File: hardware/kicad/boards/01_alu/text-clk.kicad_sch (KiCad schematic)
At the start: 8 parts, among them U287 ICM7555xB, U288 74HCT541

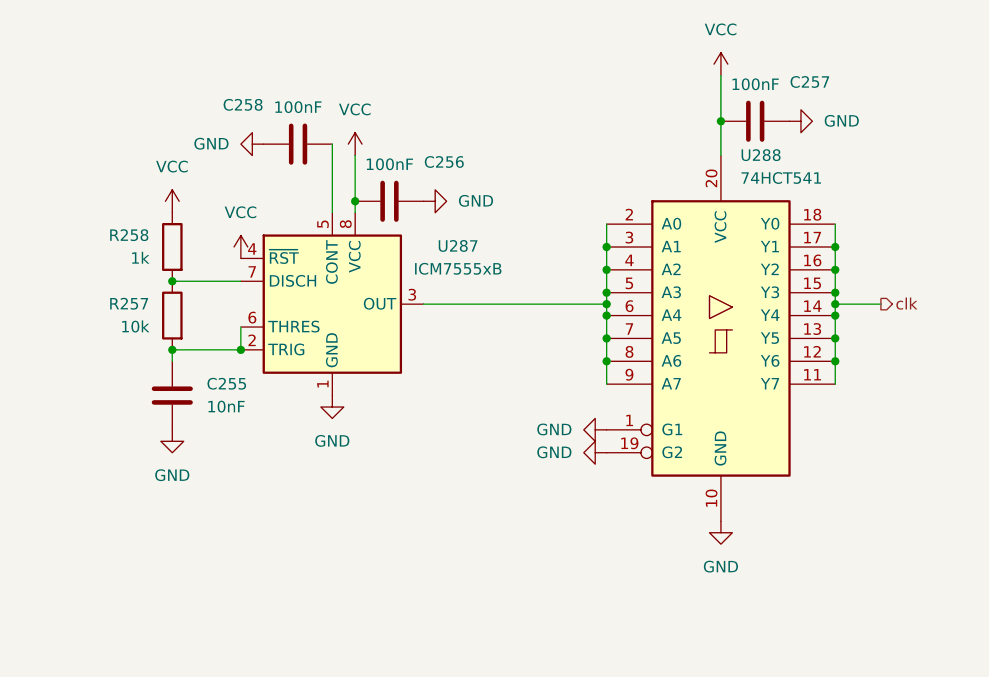
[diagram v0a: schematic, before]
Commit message: kicad: checkpoint; designed the alu display logic; clock circuit
Added registers for each display to ensure robustness and less worry about debugging screen, keeping focus on the alu board and other components
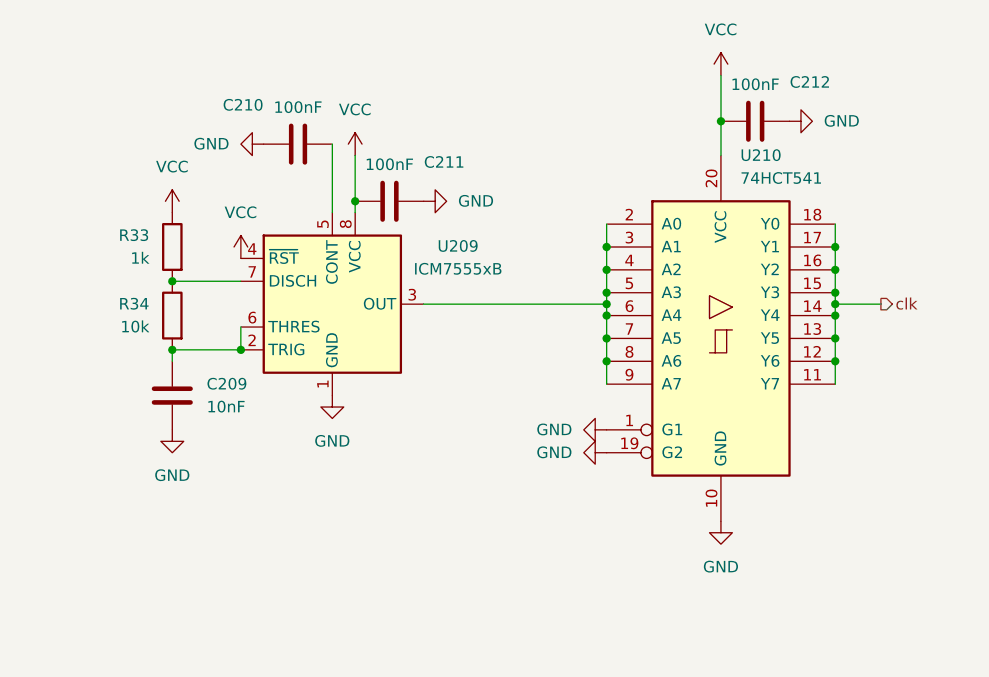
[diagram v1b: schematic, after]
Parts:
- renumbered C255 to C209, C258 to C210, C256 to C211, C257 to C212, R258 to R33, R257 to R34, U287 to U209, U288 to U210
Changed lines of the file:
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@@
 		(instances
 			(project "alu-32b"
-				(path "/ddad1417-0afc-402d-a021-92fc87ddd78a/6de98612-1f6c-44a2-b1a6-09346f0d4282/54a30aeb-1148-4a28-8e36-f59c82c9762f"
+				(path "/ddad1417-0afc-402d-a021-92fc87ddd78a/70179ff6-7c16-4036-adf3-4ea9b5e0a238/54a30aeb-1148-4a28-8e36-f59c82c9762f"
 					(reference "#PWR01036")
 					(unit 1)
@@
 		(dnp no)
 		(fields_autoplaced yes)
-		(property "Reference" "U288"
+		(property "Reference" "U210"
 			(at 173.5933 43.18 0)
 			(show_name no)
@@
 		(instances
 			(project "alu-32b"
-				(path "/ddad1417-0afc-402d-a021-92fc87ddd78a/6de98612-1f6c-44a2-b1a6-09346f0d4282/54a30aeb-1148-4a28-8e36-f59c82c9762f"
-					(reference "U288")
+				(path "/ddad1417-0afc-402d-a021-92fc87ddd78a/70179ff6-7c16-4036-adf3-4ea9b5e0a238/54a30aeb-1148-4a28-8e36-f59c82c9762f"
+					(reference "U210")
 					(unit 1)
 				)
@@
 		(instances
 			(project "alu-32b"
-				(path "/ddad1417-0afc-402d-a021-92fc87ddd78a/6de98612-1f6c-44a2-b1a6-09346f0d4282/54a30aeb-1148-4a28-8e36-f59c82c9762f"
+				(path "/ddad1417-0afc-402d-a021-92fc87ddd78a/70179ff6-7c16-4036-adf3-4ea9b5e0a238/54a30aeb-1148-4a28-8e36-f59c82c9762f"
 					(reference "#PWR01042")
 					(unit 1)
@@
 		(in_pos_files yes)
 		(dnp no)
-		(property "Reference" "C258"
+		(property "Reference" "C210"
 			(at 118.364 37.592 90)
 			(show_name no)
@@
 		(instances
 			(project "alu-32b"
-				(path "/ddad1417-0afc-402d-a021-92fc87ddd78a/6de98612-1f6c-44a2-b1a6-09346f0d4282/54a30aeb-1148-4a28-8e36-f59c82c9762f"
-					(reference "C258")
+				(path "/ddad1417-0afc-402d-a021-92fc87ddd78a/70179ff6-7c16-4036-adf3-4ea9b5e0a238/54a30aeb-1148-4a28-8e36-f59c82c9762f"
+					(reference "C210")
 					(unit 1)
 				)
@@
 		(in_pos_files yes)
 		(dnp no)
-		(property "Reference" "R258"
+		(property "Reference" "R33"
 			(at 107.95 52.0699 0)
 			(show_name no)
@@
 		(instances
 			(project "alu-32b"
-				(path "/ddad1417-0afc-402d-a021-92fc87ddd78a/6de98612-1f6c-44a2-b1a6-09346f0d4282/54a30aeb-1148-4a28-8e36-f59c82c9762f"
-					(reference "R258")
+				(path "/ddad1417-0afc-402d-a021-92fc87ddd78a/70179ff6-7c16-4036-adf3-4ea9b5e0a238/54a30aeb-1148-4a28-8e36-f59c82c9762f"
+					(reference "R33")
 					(unit 1)
 				)
@@
 		(dnp no)
 		(fields_autoplaced yes)
-		(property "Reference" "U287"
+		(property "Reference" "U209"
 			(at 142.24 53.2698 0)
 			(show_name no)
@@
 		(instances
 			(project "alu-32b"
-				(path "/ddad1417-0afc-402d-a021-92fc87ddd78a/6de98612-1f6c-44a2-b1a6-09346f0d4282/54a30aeb-1148-4a28-8e36-f59c82c9762f"
-					(reference "U287")
+				(path "/ddad1417-0afc-402d-a021-92fc87ddd78a/70179ff6-7c16-4036-adf3-4ea9b5e0a238/54a30aeb-1148-4a28-8e36-f59c82c9762f"
+					(reference "U209")
 					(unit 1)
 				)
@@
 		(instances
 			(project "alu-32b"
-				(path "/ddad1417-0afc-402d-a021-92fc87ddd78a/6de98612-1f6c-44a2-b1a6-09346f0d4282/54a30aeb-1148-4a28-8e36-f59c82c9762f"
+				(path "/ddad1417-0afc-402d-a021-92fc87ddd78a/70179ff6-7c16-4036-adf3-4ea9b5e0a238/54a30aeb-1148-4a28-8e36-f59c82c9762f"
 					(reference "#PWR01031")
 					(unit 1)
@@
 		(in_pos_files yes)
 		(dnp no)
-		(property "Reference" "C257"
+		(property "Reference" "C212"
 			(at 181.356 35.052 90)
 			(show_name no)
@@
 		(instances
 			(project "alu-32b"
-				(path "/ddad1417-0afc-402d-a021-92fc87ddd78a/6de98612-1f6c-44a2-b1a6-09346f0d4282/54a30aeb-1148-4a28-8e36-f59c82c9762f"
-					(reference "C257")
+				(path "/ddad1417-0afc-402d-a021-92fc87ddd78a/70179ff6-7c16-4036-adf3-4ea9b5e0a238/54a30aeb-1148-4a28-8e36-f59c82c9762f"
+					(reference "C212")
 					(unit 1)
 				)
@@
 		(in_pos_files yes)
 		(dnp no)
-		(property "Reference" "R257"
+		(property "Reference" "R34"
 			(at 107.95 59.6899 0)
 			(show_name no)
@@
 		(instances
 			(project "alu-32b"
-				(path "/ddad1417-0afc-402d-a021-92fc87ddd78a/6de98612-1f6c-44a2-b1a6-09346f0d4282/54a30aeb-1148-4a28-8e36-f59c82c9762f"
-					(reference "R257")
+				(path "/ddad1417-0afc-402d-a021-92fc87ddd78a/70179ff6-7c16-4036-adf3-4ea9b5e0a238/54a30aeb-1148-4a28-8e36-f59c82c9762f"
+					(reference "R34")
 					(unit 1)
 				)
@@
 		(instances
 			(project "alu-32b"
-				(path "/ddad1417-0afc-402d-a021-92fc87ddd78a/6de98612-1f6c-44a2-b1a6-09346f0d4282/54a30aeb-1148-4a28-8e36-f59c82c9762f"
+				(path "/ddad1417-0afc-402d-a021-92fc87ddd78a/70179ff6-7c16-4036-adf3-4ea9b5e0a238/54a30aeb-1148-4a28-8e36-f59c82c9762f"
 					(reference "#PWR01032")
 					(unit 1)
@@
 		(instances
 			(project "alu-32b"
-				(path "/ddad1417-0afc-402d-a021-92fc87ddd78a/6de98612-1f6c-44a2-b1a6-09346f0d4282/54a30aeb-1148-4a28-8e36-f59c82c9762f"
+				(path "/ddad1417-0afc-402d-a021-92fc87ddd78a/70179ff6-7c16-4036-adf3-4ea9b5e0a238/54a30aeb-1148-4a28-8e36-f59c82c9762f"
 					(reference "#PWR01037")
 					(unit 1)
@@
 		(instances
 			(project "alu-32b"
-				(path "/ddad1417-0afc-402d-a021-92fc87ddd78a/6de98612-1f6c-44a2-b1a6-09346f0d4282/54a30aeb-1148-4a28-8e36-f59c82c9762f"
+				(path "/ddad1417-0afc-402d-a021-92fc87ddd78a/70179ff6-7c16-4036-adf3-4ea9b5e0a238/54a30aeb-1148-4a28-8e36-f59c82c9762f"
 					(reference "#PWR01039")
 					(unit 1)
@@
 		(instances
 			(project "alu-32b"
-				(path "/ddad1417-0afc-402d-a021-92fc87ddd78a/6de98612-1f6c-44a2-b1a6-09346f0d4282/54a30aeb-1148-4a28-8e36-f59c82c9762f"
+				(path "/ddad1417-0afc-402d-a021-92fc87ddd78a/70179ff6-7c16-4036-adf3-4ea9b5e0a238/54a30aeb-1148-4a28-8e36-f59c82c9762f"
 					(reference "#PWR01040")
 					(unit 1)
@@
 		(instances
 			(project "alu-32b"
-				(path "/ddad1417-0afc-402d-a021-92fc87ddd78a/6de98612-1f6c-44a2-b1a6-09346f0d4282/54a30aeb-1148-4a28-8e36-f59c82c9762f"
+				(path "/ddad1417-0afc-402d-a021-92fc87ddd78a/70179ff6-7c16-4036-adf3-4ea9b5e0a238/54a30aeb-1148-4a28-8e36-f59c82c9762f"
 					(reference "#PWR01034")
 					(unit 1)
@@
 		(instances
 			(project "alu-32b"
-				(path "/ddad1417-0afc-402d-a021-92fc87ddd78a/6de98612-1f6c-44a2-b1a6-09346f0d4282/54a30aeb-1148-4a28-8e36-f59c82c9762f"
+				(path "/ddad1417-0afc-402d-a021-92fc87ddd78a/70179ff6-7c16-4036-adf3-4ea9b5e0a238/54a30aeb-1148-4a28-8e36-f59c82c9762f"
 					(reference "#PWR01033")
 					(unit 1)
@@
 		(instances
 			(project "alu-32b"
-				(path "/ddad1417-0afc-402d-a021-92fc87ddd78a/6de98612-1f6c-44a2-b1a6-09346f0d4282/54a30aeb-1148-4a28-8e36-f59c82c9762f"
+				(path "/ddad1417-0afc-402d-a021-92fc87ddd78a/70179ff6-7c16-4036-adf3-4ea9b5e0a238/54a30aeb-1148-4a28-8e36-f59c82c9762f"
 					(reference "#PWR01038")
 					(unit 1)
@@
 		(instances
 			(project "alu-32b"
-				(path "/ddad1417-0afc-402d-a021-92fc87ddd78a/6de98612-1f6c-44a2-b1a6-09346f0d4282/54a30aeb-1148-4a28-8e36-f59c82c9762f"
+				(path "/ddad1417-0afc-402d-a021-92fc87ddd78a/70179ff6-7c16-4036-adf3-4ea9b5e0a238/54a30aeb-1148-4a28-8e36-f59c82c9762f"
 					(reference "#PWR01041")
 					(unit 1)
@@
 		(dnp no)
 		(fields_autoplaced yes)
-		(property "Reference" "C255"
+		(property "Reference" "C209"
 			(at 114.3 68.5799 0)
 			(show_name no)
@@
 		(instances
 			(project "alu-32b"
-				(path "/ddad1417-0afc-402d-a021-92fc87ddd78a/6de98612-1f6c-44a2-b1a6-09346f0d4282/54a30aeb-1148-4a28-8e36-f59c82c9762f"
-					(reference "C255")
+				(path "/ddad1417-0afc-402d-a021-92fc87ddd78a/70179ff6-7c16-4036-adf3-4ea9b5e0a238/54a30aeb-1148-4a28-8e36-f59c82c9762f"
+					(reference "C209")
 					(unit 1)
 				)
@@
 		(in_pos_files yes)
 		(dnp no)
-		(property "Reference" "C256"
+		(property "Reference" "C211"
 			(at 140.716 43.942 90)
 			(show_name no)
@@
 		(instances
 			(project "alu-32b"
-				(path "/ddad1417-0afc-402d-a021-92fc87ddd78a/6de98612-1f6c-44a2-b1a6-09346f0d4282/54a30aeb-1148-4a28-8e36-f59c82c9762f"
-					(reference "C256")
+				(path "/ddad1417-0afc-402d-a021-92fc87ddd78a/70179ff6-7c16-4036-adf3-4ea9b5e0a238/54a30aeb-1148-4a28-8e36-f59c82c9762f"
+					(reference "C211")
 					(unit 1)
 				)
@@
 		(instances
 			(project "alu-32b"
-				(path "/ddad1417-0afc-402d-a021-92fc87ddd78a/6de98612-1f6c-44a2-b1a6-09346f0d4282/54a30aeb-1148-4a28-8e36-f59c82c9762f"
+				(path "/ddad1417-0afc-402d-a021-92fc87ddd78a/70179ff6-7c16-4036-adf3-4ea9b5e0a238/54a30aeb-1148-4a28-8e36-f59c82c9762f"
 					(reference "#PWR01035")
 					(unit 1)

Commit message: alu: completed all core schematics; DRC and ERC pending 🎉
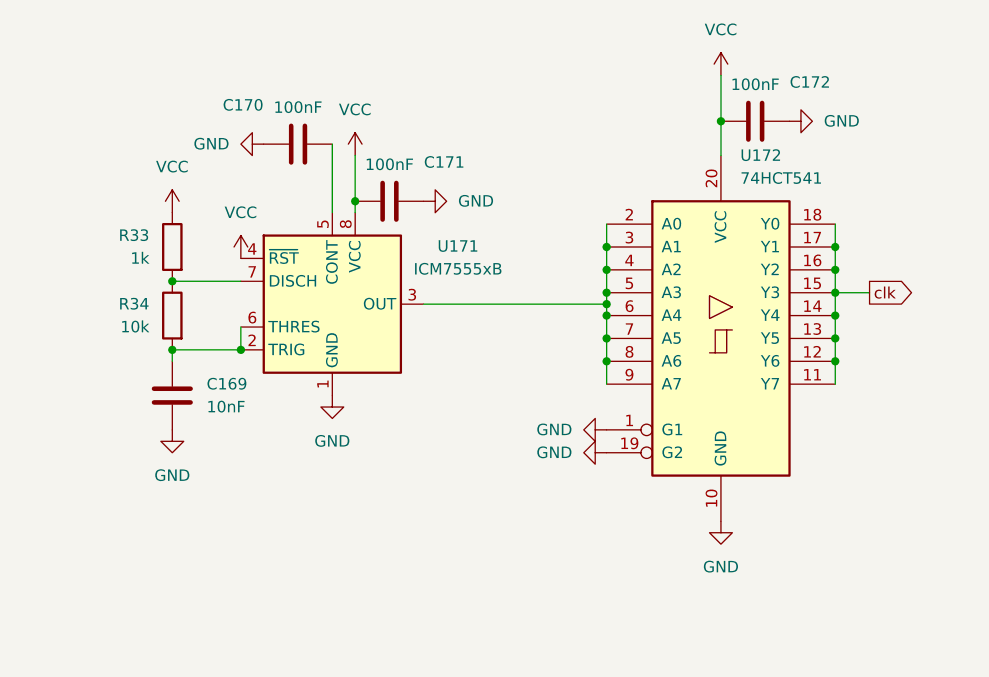
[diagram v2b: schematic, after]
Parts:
- U172: renamed from U210; footprint (none) -> Package_SO:SOIC-20W_7.5x12.8mm_P1.27mm
- renumbered C209 to C169, C210 to C170, C211 to C171, C212 to C172, U209 to U171
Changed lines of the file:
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@@
-	)
-	(junction
-		(at 184.15 59.69)
-		(diameter 0)
-		(color 0 0 0 0)
 	)
 	(junction
@@
 	(wire
 		(pts
-			(xy 184.15 59.69) (xy 184.15 60.96)
+			(xy 184.15 58.42) (xy 184.15 60.96)
 		)
 		(stroke
@@
 	(wire
 		(pts
+			(xy 184.15 58.42) (xy 187.96 58.42)
+		)
+		(stroke
+			(width 0)
+			(type default)
+		)
+	)
+	(wire
+		(pts
 			(xy 184.15 60.96) (xy 184.15 63.5)
 		)
@@
 	(wire
 		(pts
-			(xy 184.15 59.69) (xy 189.23 59.69)
-		)
-		(stroke
-			(width 0)
-			(type default)
-		)
-	)
-	(wire
-		(pts
 			(xy 158.75 59.69) (xy 158.75 60.96)
 		)
@@
 	(wire
 		(pts
-			(xy 184.15 58.42) (xy 184.15 59.69)
-		)
-		(stroke
-			(width 0)
-			(type default)
-		)
-	)
-	(wire
-		(pts
 			(xy 110.49 66.04) (xy 110.49 64.77)
 		)
@@
 		)
 	)
-	(hierarchical_label "clk"
+	(global_label "clk"
 		(shape output)
-		(at 189.23 59.69 0)
+		(at 187.96 58.42 0)
+		(fields_autoplaced yes)
 		(effects
 			(font
@@
 			(justify left)
 		)
+		(property "Intersheetrefs" "${INTERSHEET_REFS}"
+			(at 193.7271 58.42 0)
+			(hide yes)
+			(show_name no)
+			(do_not_autoplace no)
+			(effects
+				(font
+					(size 1.27 1.27)
+				)
+				(justify left)
+			)
+		)
 	)
 	(symbol
@@
 		(dnp no)
 		(fields_autoplaced yes)
-		(property "Reference" "#PWR01036"
+		(property "Reference" "#PWR0667"
 			(at 110.49 53.34 0)
 			(hide yes)
@@
 			(project "alu-32b"
 				(path "/ddad1417-0afc-402d-a021-92fc87ddd78a/70179ff6-7c16-4036-adf3-4ea9b5e0a238/54a30aeb-1148-4a28-8e36-f59c82c9762f"
-					(reference "#PWR01036")
+					(reference "#PWR0667")
 					(unit 1)
 				)
@@
 		(dnp no)
 		(fields_autoplaced yes)
-		(property "Reference" "U210"
+		(property "Reference" "U172"
 			(at 173.5933 43.18 0)
 			(show_name no)
@@
 			)
 		)
-		(property "Footprint" ""
+		(property "Footprint" "Package_SO:SOIC-20W_7.5x12.8mm_P1.27mm"
 			(at 171.45 63.5 0)
 			(hide yes)
@@
 			(project "alu-32b"
 				(path "/ddad1417-0afc-402d-a021-92fc87ddd78a/70179ff6-7c16-4036-adf3-4ea9b5e0a238/54a30aeb-1148-4a28-8e36-f59c82c9762f"
-					(reference "U210")
+					(reference "U172")
 					(unit 1)
 				)
@@
 		(dnp no)
 		(fields_autoplaced yes)
-		(property "Reference" "#PWR01042"
+		(property "Reference" "#PWR0670"
 			(at 114.3 41.91 0)
 			(hide yes)
@@
 			(project "alu-32b"
 				(path "/ddad1417-0afc-402d-a021-92fc87ddd78a/70179ff6-7c16-4036-adf3-4ea9b5e0a238/54a30aeb-1148-4a28-8e36-f59c82c9762f"
-					(reference "#PWR01042")
+					(reference "#PWR0670")
 					(unit 1)
 				)
@@
 		(in_pos_files yes)
 		(dnp no)
-		(property "Reference" "C210"
+		(property "Reference" "C170"
 			(at 118.364 37.592 90)
 			(show_name no)
@@
 			(project "alu-32b"
 				(path "/ddad1417-0afc-402d-a021-92fc87ddd78a/70179ff6-7c16-4036-adf3-4ea9b5e0a238/54a30aeb-1148-4a28-8e36-f59c82c9762f"
-					(reference "C210")
+					(reference "C170")
 					(unit 1)
 				)
@@
 		(dnp no)
 		(fields_autoplaced yes)
-		(property "Reference" "U209"
+		(property "Reference" "U171"
 			(at 142.24 53.2698 0)
 			(show_name no)
@@
 			(project "alu-32b"
 				(path "/ddad1417-0afc-402d-a021-92fc87ddd78a/70179ff6-7c16-4036-adf3-4ea9b5e0a238/54a30aeb-1148-4a28-8e36-f59c82c9762f"
-					(reference "U209")
+					(reference "U171")
 					(unit 1)
 				)
@@
 		(dnp no)
 		(fields_autoplaced yes)
-		(property "Reference" "#PWR01031"
+		(property "Reference" "#PWR0671"
 			(at 128.27 76.2 0)
 			(hide yes)
@@
 			(project "alu-32b"
 				(path "/ddad1417-0afc-402d-a021-92fc87ddd78a/70179ff6-7c16-4036-adf3-4ea9b5e0a238/54a30aeb-1148-4a28-8e36-f59c82c9762f"
-					(reference "#PWR01031")
+					(reference "#PWR0671")
 					(unit 1)
 				)
@@
 		(in_pos_files yes)
 		(dnp no)
-		(property "Reference" "C212"
+		(property "Reference" "C172"
 			(at 181.356 35.052 90)
 			(show_name no)
@@
 			(project "alu-32b"
 				(path "/ddad1417-0afc-402d-a021-92fc87ddd78a/70179ff6-7c16-4036-adf3-4ea9b5e0a238/54a30aeb-1148-4a28-8e36-f59c82c9762f"
-					(reference "C212")
+					(reference "C172")
 					(unit 1)
 				)
@@
 		(dnp no)
 		(fields_autoplaced yes)
-		(property "Reference" "#PWR01032"
+		(property "Reference" "#PWR0669"
 			(at 118.11 58.42 0)
 			(hide yes)
@@
 			(project "alu-32b"
 				(path "/ddad1417-0afc-402d-a021-92fc87ddd78a/70179ff6-7c16-4036-adf3-4ea9b5e0a238/54a30aeb-1148-4a28-8e36-f59c82c9762f"
-					(reference "#PWR01032")
+					(reference "#PWR0669")
 					(unit 1)
 				)
@@
 		(dnp no)
 		(fields_autoplaced yes)
-		(property "Reference" "#PWR01037"
+		(property "Reference" "#PWR0677"
 			(at 171.45 90.17 0)
 			(hide yes)
@@
 			(project "alu-32b"
 				(path "/ddad1417-0afc-402d-a021-92fc87ddd78a/70179ff6-7c16-4036-adf3-4ea9b5e0a238/54a30aeb-1148-4a28-8e36-f59c82c9762f"
-					(reference "#PWR01037")
+					(reference "#PWR0677")
 					(unit 1)
 				)
@@
 		(dnp no)
 		(fields_autoplaced yes)
-		(property "Reference" "#PWR01039"
+		(property "Reference" "#PWR0675"
 			(at 152.4 76.2 0)
 			(hide yes)
@@
 			(project "alu-32b"
 				(path "/ddad1417-0afc-402d-a021-92fc87ddd78a/70179ff6-7c16-4036-adf3-4ea9b5e0a238/54a30aeb-1148-4a28-8e36-f59c82c9762f"
-					(reference "#PWR01039")
+					(reference "#PWR0675")
 					(unit 1)
 				)
@@
 		(dnp no)
 		(fields_autoplaced yes)
-		(property "Reference" "#PWR01040"
+		(property "Reference" "#PWR0676"
 			(at 171.45 38.1 0)
 			(hide yes)
@@
 			(project "alu-32b"
 				(path "/ddad1417-0afc-402d-a021-92fc87ddd78a/70179ff6-7c16-4036-adf3-4ea9b5e0a238/54a30aeb-1148-4a28-8e36-f59c82c9762f"
-					(reference "#PWR01040")
+					(reference "#PWR0676")
 					(unit 1)
 				)
@@
 		(dnp no)
 		(fields_autoplaced yes)
-		(property "Reference" "#PWR01034"
+		(property "Reference" "#PWR0673"
 			(at 144.78 48.26 0)
 			(hide yes)
@@
 			(project "alu-32b"
 				(path "/ddad1417-0afc-402d-a021-92fc87ddd78a/70179ff6-7c16-4036-adf3-4ea9b5e0a238/54a30aeb-1148-4a28-8e36-f59c82c9762f"
-					(reference "#PWR01034")
+					(reference "#PWR0673")
 					(unit 1)
 				)
@@
 		(dnp no)
 		(fields_autoplaced yes)
-		(property "Reference" "#PWR01033"
+		(property "Reference" "#PWR0672"
 			(at 130.81 46.99 0)
 			(hide yes)
@@
 			(project "alu-32b"
 				(path "/ddad1417-0afc-402d-a021-92fc87ddd78a/70179ff6-7c16-4036-adf3-4ea9b5e0a238/54a30aeb-1148-4a28-8e36-f59c82c9762f"
-					(reference "#PWR01033")
+					(reference "#PWR0672")
 					(unit 1)
 				)
@@
 		(dnp no)
 		(fields_autoplaced yes)
-		(property "Reference" "#PWR01038"
+		(property "Reference" "#PWR0674"
 			(at 152.4 73.66 0)
 			(hide yes)
@@
 			(project "alu-32b"
 				(path "/ddad1417-0afc-402d-a021-92fc87ddd78a/70179ff6-7c16-4036-adf3-4ea9b5e0a238/54a30aeb-1148-4a28-8e36-f59c82c9762f"
-					(reference "#PWR01038")
+					(reference "#PWR0674")
 					(unit 1)
 				)
@@
 		(dnp no)
 		(fields_autoplaced yes)
-		(property "Reference" "#PWR01041"
+		(property "Reference" "#PWR0678"
 			(at 185.42 39.37 0)
 			(hide yes)
@@
 			(project "alu-32b"
 				(path "/ddad1417-0afc-402d-a021-92fc87ddd78a/70179ff6-7c16-4036-adf3-4ea9b5e0a238/54a30aeb-1148-4a28-8e36-f59c82c9762f"
-					(reference "#PWR01041")
+					(reference "#PWR0678")
 					(unit 1)
 				)
@@
 		(dnp no)
 		(fields_autoplaced yes)
-		(property "Reference" "C209"
+		(property "Reference" "C169"
 			(at 114.3 68.5799 0)
 			(show_name no)
@@
 			(project "alu-32b"
 				(path "/ddad1417-0afc-402d-a021-92fc87ddd78a/70179ff6-7c16-4036-adf3-4ea9b5e0a238/54a30aeb-1148-4a28-8e36-f59c82c9762f"
-					(reference "C209")
+					(reference "C169")
 					(unit 1)
 				)
@@
 		(in_pos_files yes)
 		(dnp no)
-		(property "Reference" "C211"
+		(property "Reference" "C171"
 			(at 140.716 43.942 90)
 			(show_name no)
@@
 			(project "alu-32b"
 				(path "/ddad1417-0afc-402d-a021-92fc87ddd78a/70179ff6-7c16-4036-adf3-4ea9b5e0a238/54a30aeb-1148-4a28-8e36-f59c82c9762f"
-					(reference "C211")
+					(reference "C171")
 					(unit 1)
 				)
@@
 		(dnp no)
 		(fields_autoplaced yes)
-		(property "Reference" "#PWR01035"
+		(property "Reference" "#PWR0668"
 			(at 110.49 80.01 0)
 			(hide yes)
@@
 			(project "alu-32b"
 				(path "/ddad1417-0afc-402d-a021-92fc87ddd78a/70179ff6-7c16-4036-adf3-4ea9b5e0a238/54a30aeb-1148-4a28-8e36-f59c82c9762f"
-					(reference "#PWR01035")
-					(unit 1)
-				)
+					(reference "#PWR0668")
+					(unit 1)
+				)

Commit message: refactor: improved global labeling and reduced ERC from 300+ to 6 power flags and minor connector in errors
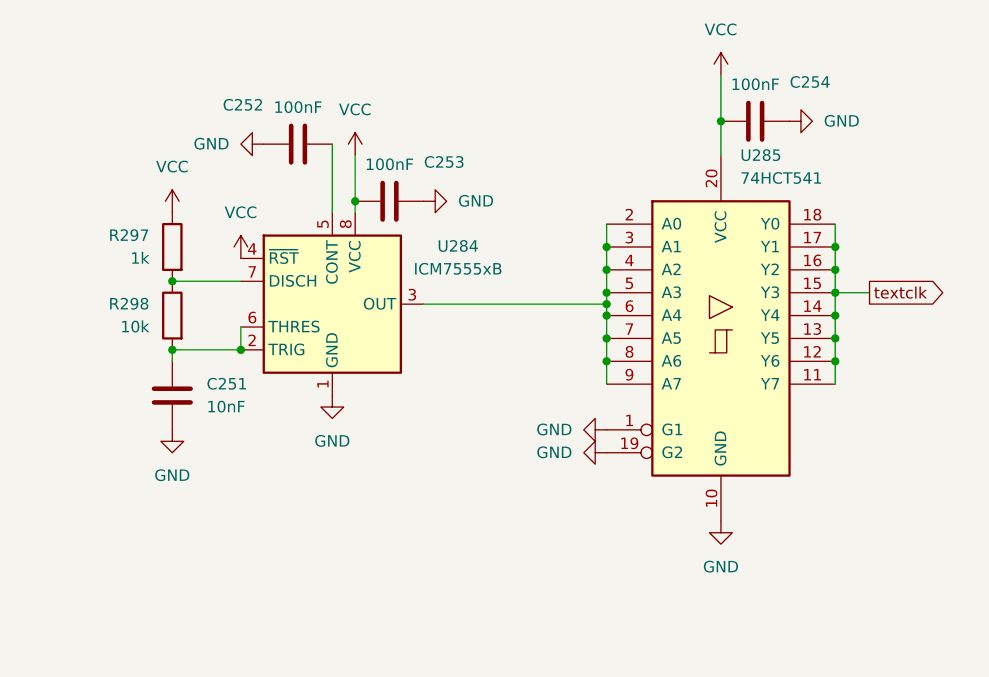
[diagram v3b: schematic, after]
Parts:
- renumbered C169 to C251, C170 to C252, C171 to C253, C172 to C254, R33 to R297, R34 to R298, U171 to U284, U172 to U285
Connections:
- net clk renamed textclk
